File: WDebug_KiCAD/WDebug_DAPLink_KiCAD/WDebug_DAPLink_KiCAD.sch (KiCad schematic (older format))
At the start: 38 parts, among them J1 Conn_01x04, J2 Conn_02x04_UART_SW, J3 Conn_01x20_Female, J4 Conn_01x05_Male, J5 01x18_Female_Fan, P1 USB_C_Plug_USB2.0, SW1 SW_Rst, U1 AZ1117-3.3, U2 STM32F103C8Tx, Y1 8MHz

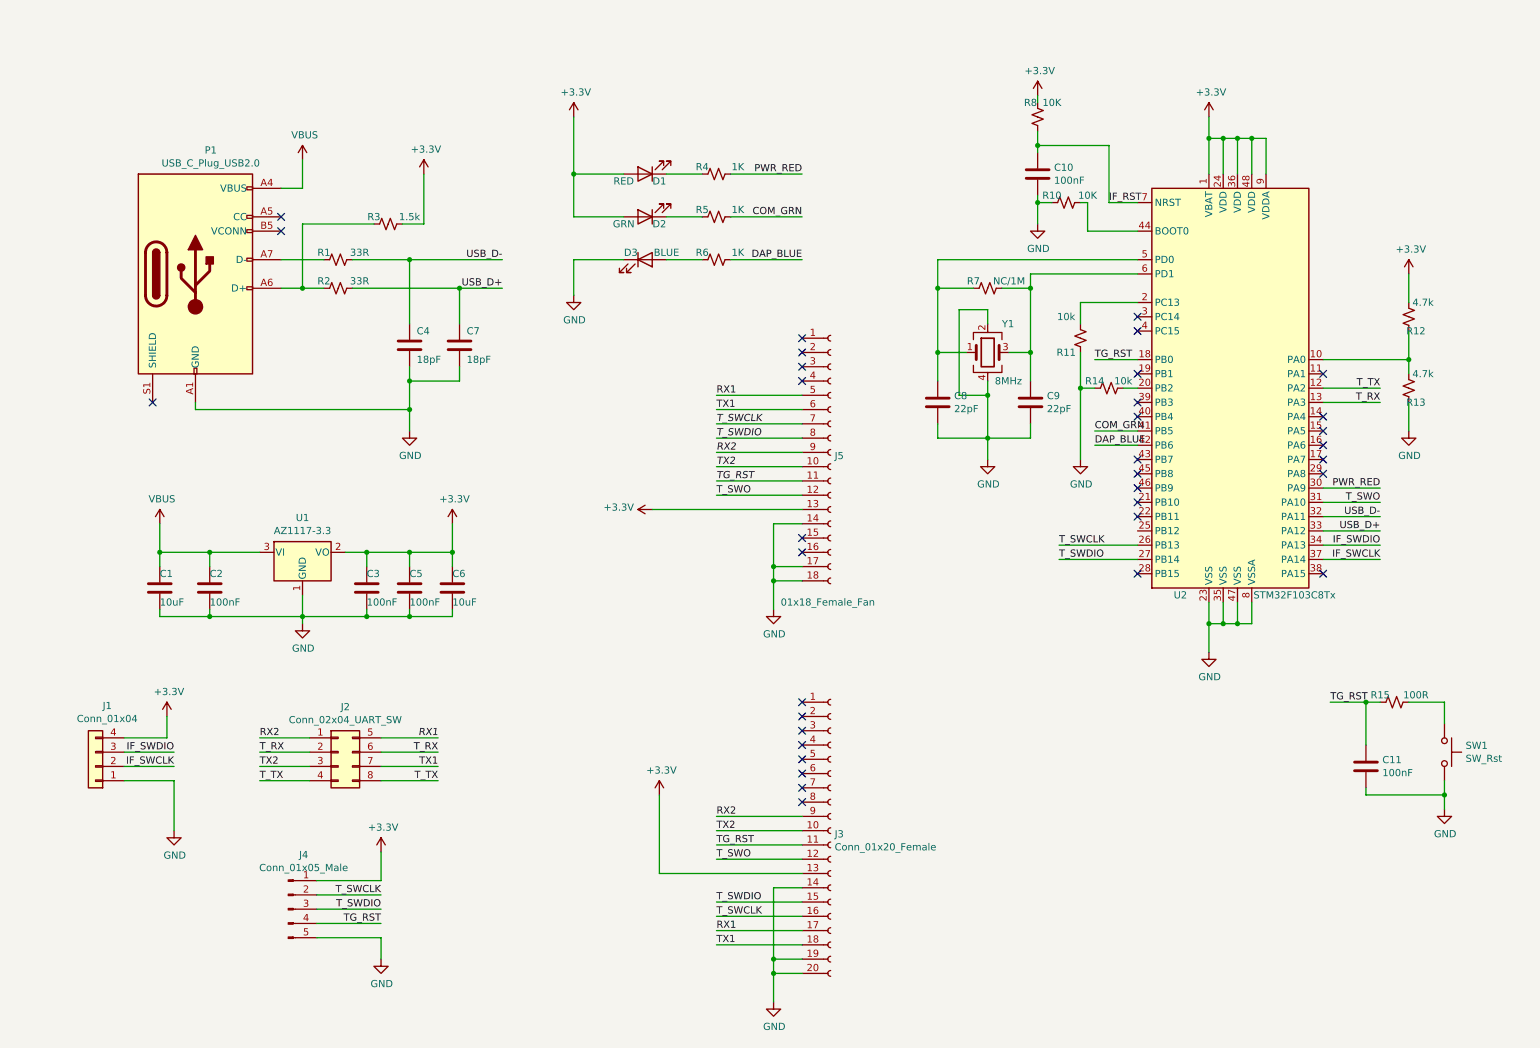
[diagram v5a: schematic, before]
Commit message: WDebug_DAPLink V1.4 1 修改 16Pin接口SWCLK和SWDIO反了。 2 3.3V不直接连接到16pin和18pin接口 3 AMS1117换成线性3819
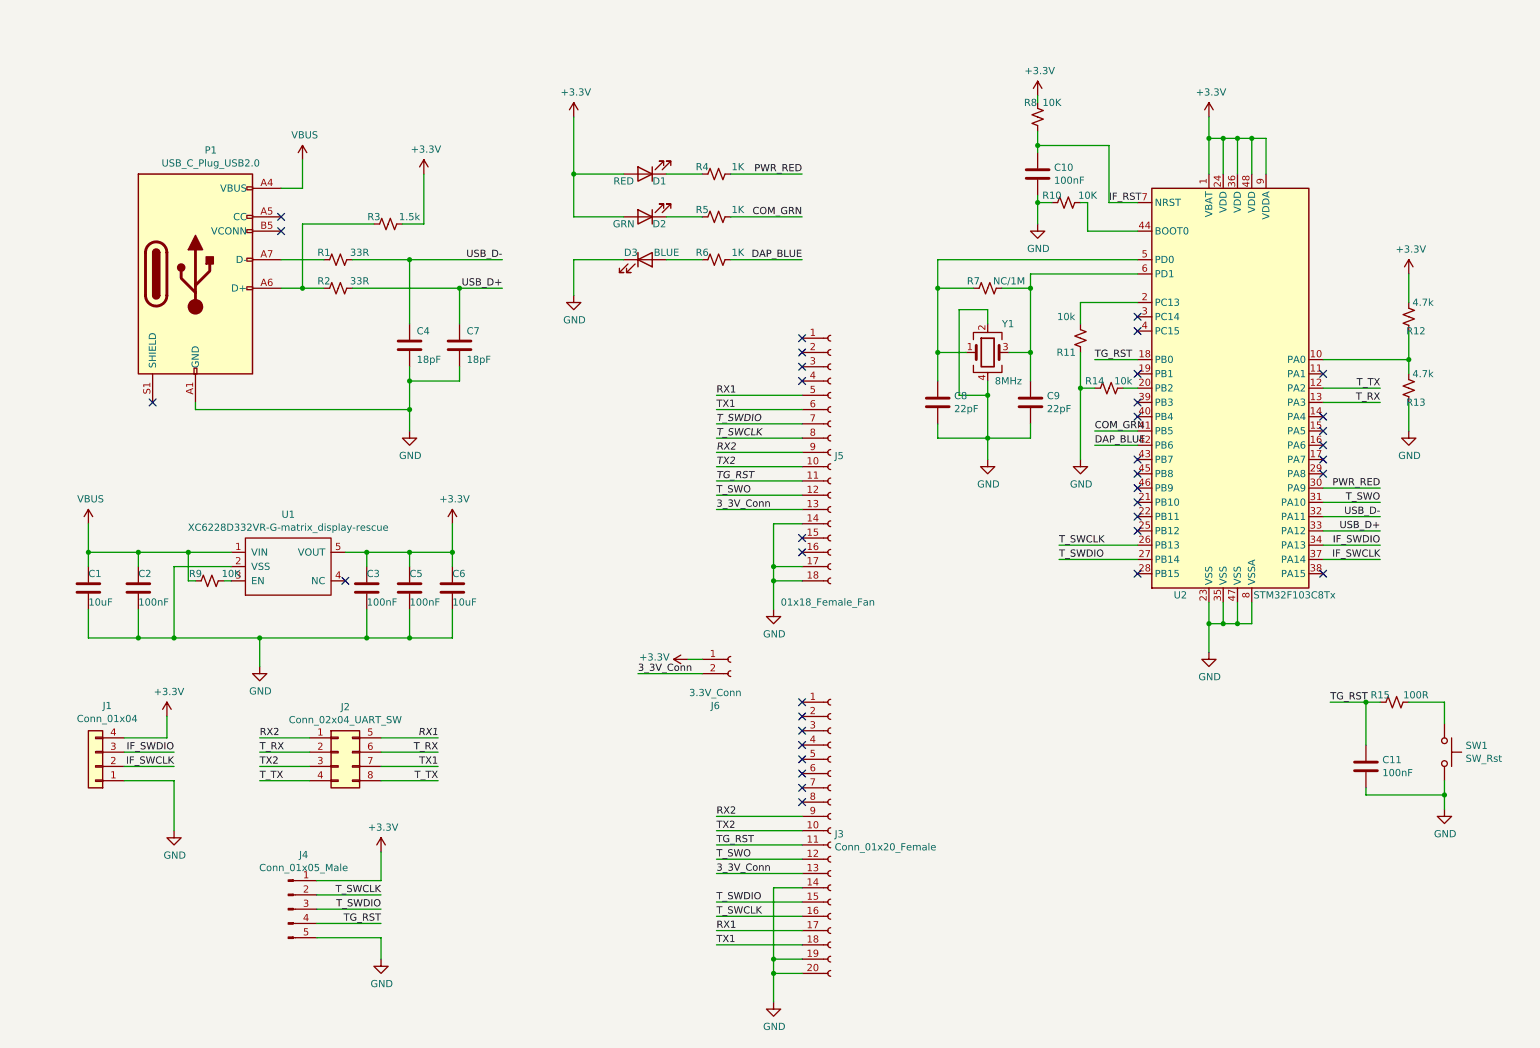
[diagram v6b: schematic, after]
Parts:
- removed U1: AZ1117-3.3, Package_TO_SOT_SMD:SOT-223, symbol WDebug_DAPLink_KiCAD-rescue:AZ1117-3.3-Regulator_Linear
- added J6: 3.3V_Conn, Connector_PinHeader_2.54mm:PinHeader_1x02_P2.54mm_Vertical, symbol Connector:Conn_01x02_Female
- added R9: 10K, Resistor_SMD:R_0603_1608Metric, symbol WDebug_DAPLink_KiCAD-rescue:R_Small_US-Device
- added U1: XC6228D332VR-G-matrix_display-rescue, matrix_control_main:SOT23-5, symbol matrix_control_main-rescue:XC6228D332VR-G-matrix_display-rescue
- Y1: footprint Crystal:Crystal_SMD_3225-4Pin_3.2x2.5mm -> Crystal:Crystal_SMD_5032-4Pin_5.0x3.2mm
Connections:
- net +3V3: now also J6.1 (Pin_1), U1.5 (VOUT); no longer J3.13 (Pin_13), J5.13 (Pin_13)
- net GND: now also U1.2 (VSS)
- net T_SWCLK: now also J5.8 (Pin_8); no longer J5.7 (Pin_7)
- net T_SWDIO: now also J5.7 (Pin_7); no longer J5.8 (Pin_8)
- net VBUS: now also R9.2, U1.1 (VIN)
- new net: R9.1, U1.3 (EN)
- new net 3_3V_Conn: J3.13 (Pin_13), J5.13 (Pin_13), J6.2 (Pin_2)
- no-connect marks 35 -> 37
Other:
- moved on the sheet: C1, C2
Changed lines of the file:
@@
 	-1   0    0    1
 $EndComp
-$Comp
-L WDebug_DAPLink_KiCAD-rescue:C-Device C2
-U 1 1 5E0EA74B
-P 1800 4550
-F 0 "C2" H 1800 4650 50  0000 L CNN
-F 1 "100nF" H 1800 4450 50  0000 L CNN
-F 2 "Capacitor_SMD:C_0603_1608Metric" H 1838 4400 50  0001 C CNN
-F 3 "~" H 1800 4550 50  0001 C CNN
-	1    1800 4550
-	1    0    0    -1
-$EndComp
-Wire Wire Line
-	2900 4750 2450 4750
-Connection ~ 2900 4750
-Wire Wire Line
-	2900 4700 2900 4750
 Wire Wire Line
 	2900 4300 3200 4300
@@
 	2900 4400 2900 4300
 Wire Wire Line
-	3200 4750 2900 4750
-Connection ~ 3200 4750
-Wire Wire Line
-	3200 4700 3200 4750
-Wire Wire Line
 	3200 4300 3500 4300
 Connection ~ 3200 4300
 Wire Wire Line
 	3200 4400 3200 4300
-Wire Wire Line
-	3500 4750 3200 4750
-Wire Wire Line
-	3500 4700 3500 4750
 Connection ~ 3500 4300
 Wire Wire Line
 	3500 4300 3500 4400
 Wire Wire Line
-	1800 4300 2150 4300
-Connection ~ 1800 4300
-Wire Wire Line
-	1800 4400 1800 4300
-Wire Wire Line
-	1800 4750 2450 4750
-Connection ~ 1800 4750
-Wire Wire Line
-	1800 4700 1800 4750
-Wire Wire Line
-	2450 4750 2450 4800
-Connection ~ 2450 4750
-Wire Wire Line
-	1450 4750 1800 4750
-Wire Wire Line
-	1450 4700 1450 4750
-Connection ~ 1450 4300
-Wire Wire Line
-	1450 4300 1450 4400
-Wire Wire Line
-	2450 4600 2450 4750
+	1300 4400 1300 4300
+Wire Wire Line
+	950  4900 1300 4900
+Connection ~ 950  4300
+Wire Wire Line
+	950  4300 950  4400
 $Comp
 L WDebug_DAPLink_KiCAD-rescue:GND-power #PWR0117
 U 1 1 5E279A9C
-P 2450 4800
-F 0 "#PWR0117" H 2450 4550 50  0001 C CNN
-F 1 "GND" H 2455 4627 50  0000 C CNN
-F 2 "" H 2450 4800 50  0001 C CNN
-F 3 "" H 2450 4800 50  0001 C CNN
-	1    2450 4800
+P 2150 5100
+F 0 "#PWR0117" H 2150 4850 50  0001 C CNN
+F 1 "GND" H 2155 4927 50  0000 C CNN
+F 2 "" H 2150 5100 50  0001 C CNN
+F 3 "" H 2150 5100 50  0001 C CNN
+	1    2150 5100
 	1    0    0    -1
 $EndComp
@@
 	2750 4300 2900 4300
 Wire Wire Line
-	1450 4300 1800 4300
-Wire Wire Line
-	1450 4100 1450 4300
+	950  4300 1300 4300
+Wire Wire Line
+	950  4100 950  4300
 $Comp
 L WDebug_DAPLink_KiCAD-rescue:VBUS-power #PWR0116
 U 1 1 5E27AB27
-P 1450 4100
-F 0 "#PWR0116" H 1450 3950 50  0001 C CNN
-F 1 "VBUS" H 1465 4273 50  0000 C CNN
-F 2 "" H 1450 4100 50  0001 C CNN
-F 3 "" H 1450 4100 50  0001 C CNN
-	1    1450 4100
+P 950 4100
+F 0 "#PWR0116" H 950 3950 50  0001 C CNN
+F 1 "VBUS" H 965 4273 50  0000 C CNN
+F 2 "" H 950 4100 50  0001 C CNN
+F 3 "" H 950 4100 50  0001 C CNN
+	1    950  4100
 	1    0    0    -1
 $EndComp
@@
 F 3 "" H 3500 4100 50  0001 C CNN
 	1    3500 4100
-	1    0    0    -1
-$EndComp
-$Comp
-L WDebug_DAPLink_KiCAD-rescue:AZ1117-3.3-Regulator_Linear U1
-U 1 1 5E278830
-P 2450 4300
-F 0 "U1" H 2450 4542 50  0000 C CNN
-F 1 "AZ1117-3.3" H 2450 4451 50  0000 C CNN
-F 2 "Package_TO_SOT_SMD:SOT-223" H 2450 4550 50  0001 C CIN
-F 3 "https://www.diodes.com/assets/Datasheets/AZ1117.pdf" H 2450 4300 50  0001 C CNN
-	1    2450 4300
 	1    0    0    -1
 $EndComp
@@
 $EndComp
 $Comp
-L WDebug_DAPLink_KiCAD-rescue:C-Device C6
-U 1 1 5E0EB136
-P 3500 4550
-F 0 "C6" H 3500 4650 50  0000 L CNN
-F 1 "10uF" H 3500 4450 50  0000 L CNN
-F 2 "Capacitor_SMD:C_0603_1608Metric" H 3538 4400 50  0001 C CNN
-F 3 "~" H 3500 4550 50  0001 C CNN
-	1    3500 4550
-	1    0    0    -1
-$EndComp
-$Comp
-L WDebug_DAPLink_KiCAD-rescue:C-Device C5
-U 1 1 5E0EAE03
-P 3200 4550
-F 0 "C5" H 3200 4650 50  0000 L CNN
-F 1 "100nF" H 3200 4450 50  0000 L CNN
-F 2 "Capacitor_SMD:C_0603_1608Metric" H 3238 4400 50  0001 C CNN
-F 3 "~" H 3200 4550 50  0001 C CNN
-	1    3200 4550
-	1    0    0    -1
-$EndComp
-$Comp
-L WDebug_DAPLink_KiCAD-rescue:C-Device C3
-U 1 1 5E0EAA88
-P 2900 4550
-F 0 "C3" H 2900 4650 50  0000 L CNN
-F 1 "100nF" H 2900 4450 50  0000 L CNN
-F 2 "Capacitor_SMD:C_0603_1608Metric" H 2938 4400 50  0001 C CNN
-F 3 "~" H 2900 4550 50  0001 C CNN
-	1    2900 4550
-	1    0    0    -1
-$EndComp
-$Comp
 L WDebug_DAPLink_KiCAD-rescue:C-Device C10
 U 1 1 5E0EA4DE
@@
 $EndComp
 $Comp
-L WDebug_DAPLink_KiCAD-rescue:C-Device C1
-U 1 1 5E0E976F
-P 1450 4550
-F 0 "C1" H 1450 4650 50  0000 L CNN
-F 1 "10uF" H 1450 4450 50  0000 L CNN
-F 2 "Capacitor_SMD:C_0603_1608Metric" H 1488 4400 50  0001 C CNN
-F 3 "~" H 1450 4550 50  0001 C CNN
-	1    1450 4550
-	1    0    0    -1
-$EndComp
-$Comp
 L WDebug_DAPLink_KiCAD-rescue:C-Device C8
 U 1 1 5E0E8290
@@
 F 0 "Y1" H 7350 3100 50  0000 L CNN
 F 1 "8MHz" H 7300 2700 50  0000 L CNN
-F 2 "Crystal:Crystal_SMD_3225-4Pin_3.2x2.5mm" H 7250 2900 50  0001 C CNN
+F 2 "Crystal:Crystal_SMD_5032-4Pin_5.0x3.2mm" H 7250 2900 50  0001 C CNN
 F 3 "~" H 7250 2900 50  0001 C CNN
 	1    7250 2900
@@
 	5950 3800 5350 3800
 Wire Wire Line
-	5950 4000 4900 4000
-Wire Wire Line
 	5950 4100 5750 4100
 Wire Wire Line
@@
 	1    5750 4700
 	1    0    0    -1
-$EndComp
-$Comp
-L WDebug_DAPLink_KiCAD-rescue:+3.3V-power #PWR0104
-U 1 1 5E9EB13C
-P 4900 4000
-F 0 "#PWR0104" H 4900 3850 50  0001 C CNN
-F 1 "+3.3V" V 4915 4128 50  0000 L CNN
-F 2 "" H 4900 4000 50  0001 C CNN
-F 3 "" H 4900 4000 50  0001 C CNN
-	1    4900 4000
-	0    -1   -1   0
 $EndComp
 Wire Wire Line
@@
 TX2
 Text Label 5350 3400 0    50   Italic 0
+T_SWDIO
+Text Label 5350 3500 0    50   Italic 0
 T_SWCLK
-Text Label 5350 3500 0    50   Italic 0
-T_SWDIO
 Text Label 5350 3800 0    50   Italic 0
 TG_RST
@@
 T_SWO
 $Comp
-L WDebug_DAPLink_KiCAD-rescue:+3.3V-power #PWR0124
-U 1 1 5EA83DB7
-P 4950 6000
-F 0 "#PWR0124" H 4950 5850 50  0001 C CNN
-F 1 "+3.3V" H 4965 6173 50  0000 C CNN
-F 2 "" H 4950 6000 50  0001 C CNN
-F 3 "" H 4950 6000 50  0001 C CNN
-	1    4950 6000
-	1    0    0    -1
-$EndComp
-Wire Wire Line
-	4950 6000 4950 6550
-Wire Wire Line
-	4950 6550 5950 6550
+L matrix_control_main-rescue:XC6228D332VR-G-matrix_display-rescue U1
+U 1 1 5EC428E3
+P 2350 4400
+F 0 "U1" H 2350 4765 50  0000 C CNN
+F 1 "XC6228D332VR-G-matrix_display-rescue" H 2350 4674 50  0000 C CNN
+F 2 "matrix_control_main:SOT23-5" H 2350 4650 50  0001 C CNN
+F 3 "" H 2350 4650 50  0001 C CNN
+	1    2350 4400
+	1    0    0    -1
+$EndComp
+Wire Wire Line
+	1300 4700 1300 4900
+$Comp
+L WDebug_DAPLink_KiCAD-rescue:C-Device C1
+U 1 1 5E0E976F
+P 950 4550
+F 0 "C1" H 950 4650 50  0000 L CNN
+F 1 "10uF" H 950 4450 50  0000 L CNN
+F 2 "Capacitor_SMD:C_0603_1608Metric" H 988 4400 50  0001 C CNN
+F 3 "~" H 950 4550 50  0001 C CNN
+	1    950  4550
+	1    0    0    -1
+$EndComp
+$Comp
+L WDebug_DAPLink_KiCAD-rescue:C-Device C3
+U 1 1 5E0EAA88
+P 2900 4550
+F 0 "C3" H 2900 4650 50  0000 L CNN
+F 1 "100nF" H 2900 4450 50  0000 L CNN
+F 2 "Capacitor_SMD:C_0603_1608Metric" H 2938 4400 50  0001 C CNN
+F 3 "~" H 2900 4550 50  0001 C CNN
+	1    2900 4550
+	1    0    0    -1
+$EndComp
+$Comp
+L WDebug_DAPLink_KiCAD-rescue:C-Device C5
+U 1 1 5E0EAE03
+P 3200 4550
+F 0 "C5" H 3200 4650 50  0000 L CNN
+F 1 "100nF" H 3200 4450 50  0000 L CNN
+F 2 "Capacitor_SMD:C_0603_1608Metric" H 3238 4400 50  0001 C CNN
+F 3 "~" H 3200 4550 50  0001 C CNN
+	1    3200 4550
+	1    0    0    -1
+$EndComp
+$Comp
+L WDebug_DAPLink_KiCAD-rescue:C-Device C6
+U 1 1 5E0EB136
+P 3500 4550
+F 0 "C6" H 3500 4650 50  0000 L CNN
+F 1 "10uF" H 3500 4450 50  0000 L CNN
+F 2 "Capacitor_SMD:C_0603_1608Metric" H 3538 4400 50  0001 C CNN
+F 3 "~" H 3500 4550 50  0001 C CNN
+	1    3500 4550
+	1    0    0    -1
+$EndComp
+$Comp
+L WDebug_DAPLink_KiCAD-rescue:C-Device C2
+U 1 1 5E0EA74B
+P 1300 4550
+F 0 "C2" H 1300 4650 50  0000 L CNN
+F 1 "100nF" H 1300 4450 50  0000 L CNN
+F 2 "Capacitor_SMD:C_0603_1608Metric" H 1338 4400 50  0001 C CNN
+F 3 "~" H 1300 4550 50  0001 C CNN
+	1    1300 4550
+	1    0    0    -1
+$EndComp
+Wire Wire Line
+	1950 4300 1650 4300
+Connection ~ 1300 4300
+Wire Wire Line
+	1950 4400 1550 4400
+Wire Wire Line
+	1550 4400 1550 4900
+Wire Wire Line
+	1550 4900 1300 4900
+Connection ~ 1300 4900
+Wire Wire Line
+	950  4700 950  4900
+Wire Wire Line
+	1550 4900 2150 4900
+Wire Wire Line
+	2150 4900 2150 5100
+Connection ~ 1550 4900
+Wire Wire Line
+	3500 4900 3200 4900
+Wire Wire Line
+	3500 4700 3500 4900
+Connection ~ 2150 4900
+Wire Wire Line
+	2900 4700 2900 4900
+Connection ~ 2900 4900
+Wire Wire Line
+	2900 4900 2150 4900
+Wire Wire Line
+	3200 4700 3200 4900
+Connection ~ 3200 4900
+Wire Wire Line
+	3200 4900 2900 4900
+$Comp
+L WDebug_DAPLink_KiCAD-rescue:R_Small_US-Device R9
+U 1 1 5ED189D4
+P 1800 4500
+F 0 "R9" V 1750 4400 50  0000 C CNN
+F 1 "10K" V 1750 4650 50  0000 C CNN
+F 2 "Resistor_SMD:R_0603_1608Metric" H 1800 4500 50  0001 C CNN
+F 3 "~" H 1800 4500 50  0001 C CNN
+	1    1800 4500
+	0    1    1    0
+$EndComp
+Wire Wire Line
+	1950 4500 1900 4500
+Wire Wire Line
+	1700 4500 1650 4500
+Wire Wire Line
+	1650 4500 1650 4300
+Connection ~ 1650 4300
+Wire Wire Line
+	1650 4300 1300 4300
+NoConn ~ 8300 4150
+NoConn ~ 2750 4500
+$Comp
+L WDebug_DAPLink_KiCAD-rescue:+3.3V-power #PWR0104
+U 1 1 5E9EB13C
+P 5150 5050
+F 0 "#PWR0104" H 5150 4900 50  0001 C CNN
+F 1 "+3.3V" V 5165 5178 50  0000 L CNN
+F 2 "" H 5150 5050 50  0001 C CNN
+F 3 "" H 5150 5050 50  0001 C CNN
+	1    5150 5050
+	0    -1   -1   0
+$EndComp
+$Comp
+L Connector:Conn_01x02_Female J6
+U 1 1 5EBECC61
+P 5450 5050
+F 0 "J6" H 5342 4725 50  0000 C CNN
+F 1 "3.3V_Conn" H 5342 4816 50  0000 C CNN
+F 2 "Connector_PinHeader_2.54mm:PinHeader_1x02_P2.54mm_Vertical" H 5450 5050 50  0001 C CNN
+F 3 "~" H 5450 5050 50  0001 C CNN
+	1    5450 5050
+	1    0    0    -1
+$EndComp
+Wire Wire Line
+	5250 5050 5150 5050
+Wire Wire Line
+	5250 5150 4800 5150
+Text Label 4800 5150 0    50   ~ 0
+3_3V_Conn
+Wire Wire Line
+	5950 4000 5350 4000
+Wire Wire Line
+	5950 6550 5350 6550
+Text Label 5350 4000 0    50   ~ 0
+3_3V_Conn
+Text Label 5350 6550 0    50   ~ 0
+3_3V_Conn
 $EndSCHEMATC

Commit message: 修正DAPlink 1.5版本 串口信号修改，新加一路串口
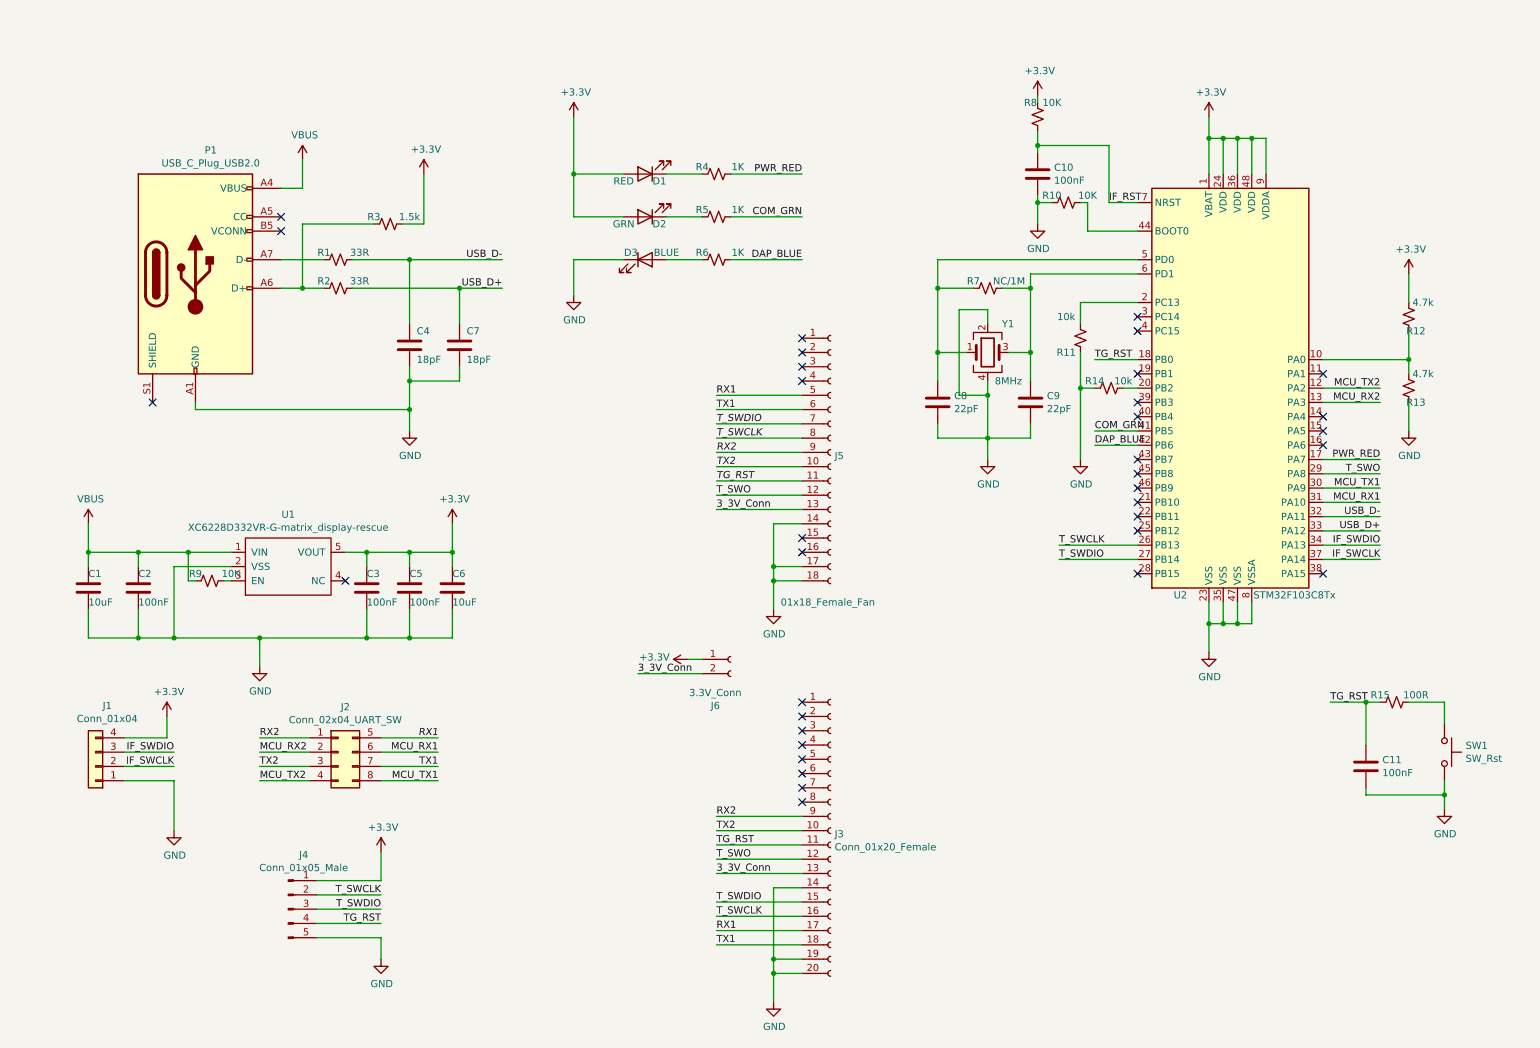
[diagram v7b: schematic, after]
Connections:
- net PWR_RED: now also U2.17 (PA7); no longer U2.30 (PA9)
- net T_SWO: now also U2.29 (PA8); no longer U2.31 (PA10)
- net T_RX renamed MCU_RX2
- net MCU_RX2: no longer J2.6 (Pin_6)
- net T_TX renamed MCU_TX2
- net MCU_TX2: no longer J2.8 (Pin_8)
- new net MCU_RX1: J2.6 (Pin_6), U2.31 (PA10)
- new net MCU_TX1: J2.8 (Pin_8), U2.30 (PA9)
- no-connect marks 37 -> 35
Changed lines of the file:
@@
 $EndComp
 Text Label 10000 3850 2    50   ~ 0
-PWR_RED
+MCU_TX1
 Text Label 10000 3950 2    50   ~ 0
-T_SWO
+MCU_RX1
 Text Label 10000 4150 2    50   ~ 0
 USB_D+
@@
 IF_SWDIO
 Text Label 10000 3250 2    50   ~ 0
-T_RX
+MCU_RX2
 Text Label 10000 3150 2    50   ~ 0
-T_TX
+MCU_TX2
 NoConn ~ 9600 4450
-NoConn ~ 9600 3750
-NoConn ~ 9600 3650
 NoConn ~ 9600 3550
 Wire Wire Line
@@
 RX1
 Text Label 3400 5700 2    50   ~ 0
-T_RX
+MCU_RX1
 Text Label 3400 5800 2    50   ~ 0
 TX1
 Text Label 3400 5900 2    50   ~ 0
-T_TX
+MCU_TX1
 Text Label 5350 3200 0    50   ~ 0
 RX1
@@
 	2500 5900 2150 5900
 Text Label 2150 5700 0    50   ~ 0
-T_RX
+MCU_RX2
 Text Label 2150 5900 0    50   ~ 0
-T_TX
+MCU_TX2
 $Comp
 L WDebug_DAPLink_KiCAD-rescue:SW_Push-Switch SW1
@@
 Text Label 5350 6550 0    50   ~ 0
 3_3V_Conn
+Wire Wire Line
+	9600 3750 10000 3750
+Wire Wire Line
+	9600 3650 10000 3650
+Text Label 10000 3650 2    50   ~ 0
+PWR_RED
+Text Label 10000 3750 2    50   ~ 0
+T_SWO
 $EndSCHEMATC
